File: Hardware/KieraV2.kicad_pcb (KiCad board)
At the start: 2 copper layers, 111 x 63.2 mm, 87 parts, among them J1 Conn_01x04_Male, J2 Conn_01x05_Male, SW1 SW_Rotary2x4, SW2 SW_Rotary2x4, SW3 SW_Push, SW4 SW_Push, SW5 SW_Push, SW6 SW_Push, SW7 SW_MEC_5G, U1 STM32L4P5RET6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

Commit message: aaaaa
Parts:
- removed MHe: MountingHole_3.2mm_M3, MountingHole:MountingHole_3.2mm_M3
- added MH6: MountingHole_3.2mm_M3, MountingHole:MountingHole_3.2mm_M3, F.Cu at (188.4, 96.0)
- renumbered MHe to MH2
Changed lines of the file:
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@@
     (tags "mounting hole 3.2mm no annular m3")
     (attr virtual)
-    (fp_text reference MHe (at -0.05 2.75) (layer F.SilkS)
+    (fp_text reference MH6 (at -0.05 2.75) (layer F.SilkS)
       (effects (font (size 1 1) (thickness 0.15)))
     )
@@
     (tags "mounting hole 4.5mm no annular")
     (attr virtual)
-    (fp_text reference MHe (at 0 6) (layer F.SilkS)
+    (fp_text reference MH2 (at 0 6) (layer F.SilkS)
       (effects (font (size 1 1) (thickness 0.15)))
     )

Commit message: added 6pin connector and somme labels
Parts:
- J2: value Conn_01x05_Male -> Conn_01x06_Male; footprint Connector_PinHeader_2.54mm:PinHeader_1x05_P2.54mm_Vertical -> Connector_PinHeader_2.54mm:PinHeader_1x06_P2.54mm_Vertical
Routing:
- net /SWO: track 0.00 -> 40.6 mm, vias 0 -> 2
- net /SW5: track 69.2 -> 71.6 mm
- net /SW6: track 71.0 -> 73.1 mm
- net GND: vias 45 -> 44
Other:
- board text added: "+5V"
- board text added: "CAN+"
- board text added: "CAN-"
- board text added: "SWO"

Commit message: added ground
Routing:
- net GND: vias 44 -> 49
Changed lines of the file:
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@@
     (thickness 1.6)
     (drawings 31)
-    (tracks 535)
+    (tracks 540)
     (zones 0)
     (modules 87)
@@
     (pcbplotparams
       (layerselection 0x010fc_ffffffff)
-      (usegerberextensions false)
+      (usegerberextensions true)
       (usegerberattributes true)
       (usegerberadvancedattributes true)
-      (creategerberjobfile true)
+      (creategerberjobfile false)
       (excludeedgelayer true)
       (linewidth 0.100000)
@@
       (psa4output false)
       (plotreference true)
-      (plotvalue true)
+      (plotvalue false)
       (plotinvisibletext false)
       (padsonsilk false)
-      (subtractmaskfromsilk false)
+      (subtractmaskfromsilk true)
       (outputformat 1)
       (mirror false)
-      (drillshape 1)
+      (drillshape 0)
       (scaleselection 1)
-      (outputdirectory ""))
+      (outputdirectory "SteeringWheelGerber/"))
   )
   (net 0 "")
@@
       (effects (font (size 1 1) (thickness 0.15)))
     )
-    (fp_text user %R (at 0 6.35) (layer F.Fab)
-      (effects (font (size 1 1) (thickness 0.15)))
-    )
     (fp_line (start -0.635 -1.27) (end 1.27 -1.27) (layer F.Fab) (width 0.1))
     (fp_line (start 1.27 -1.27) (end 1.27 13.97) (layer F.Fab) (width 0.1))
@@
     (fp_line (start 1.8 14.5) (end 1.8 -1.8) (layer F.CrtYd) (width 0.05))
     (fp_line (start 1.8 -1.8) (end -1.8 -1.8) (layer F.CrtYd) (width 0.05))
+    (fp_text user %R (at 0 6.35) (layer F.Fab)
+      (effects (font (size 1 1) (thickness 0.15)))
+    )
     (pad 6 thru_hole oval (at 0 12.7 270) (size 1.7 1.7) (drill 1) (layers *.Cu *.Mask)
       (net 45 /SWO))
@@
     (pad 2 thru_hole circle (at 4.2 0 270) (size 1.85 1.85) (drill 0.85) (layers *.Cu *.Mask)
       (net 89 /CAN+))
-    (pad 1 thru_hole roundrect (at 0 0 270) (size 1.85 1.85) (drill 0.85) (layers *.Cu *.Mask) (roundrect_rratio 0.135135)
+    (pad 1 thru_hole roundrect (at 0 0 270) (size 1.85 1.85) (drill 0.85) (layers *.Cu *.Mask) (roundrect_rratio 0.1351345945945946)
       (net 9 +5V))
     (model ${KISYS3DMOD}/Connector_Wire.3dshapes/SolderWire-0.25sqmm_1x04_P4.2mm_D0.65mm_OD1.7mm_Relief.wrl
@@
       (effects (font (size 0.5 0.5) (thickness 0.08)))
     )
-    (pad 2 smd roundrect (at 0.9625 0) (size 1.325 1.3) (layers F.Cu F.Paste F.Mask) (roundrect_rratio 0.192308)
+    (pad 2 smd roundrect (at 0.9625 0) (size 1.325 1.3) (layers F.Cu F.Paste F.Mask) (roundrect_rratio 0.1923076923076923)
       (net 95 "Net-(D7-Pad2)"))
-    (pad 1 smd roundrect (at -0.9625 0) (size 1.325 1.3) (layers F.Cu F.Paste F.Mask) (roundrect_rratio 0.192308)
+    (pad 1 smd roundrect (at -0.9625 0) (size 1.325 1.3) (layers F.Cu F.Paste F.Mask) (roundrect_rratio 0.1923076923076923)
       (net 8 +3V3))
     (model ${KISYS3DMOD}/Diode_SMD.3dshapes/D_0805_2012Metric_Castellated.wrl
@@
       (effects (font (size 0.5 0.5) (thickness 0.08)))
     )
-    (pad 2 smd roundrect (at 0.9625 0) (size 1.325 1.3) (layers F.Cu F.Paste F.Mask) (roundrect_rratio 0.192308)
+    (pad 2 smd roundrect (at 0.9625 0) (size 1.325 1.3) (layers F.Cu F.Paste F.Mask) (roundrect_rratio 0.1923076923076923)
       (net 94 "Net-(D6-Pad2)"))
-    (pad 1 smd roundrect (at -0.9625 0) (size 1.325 1.3) (layers F.Cu F.Paste F.Mask) (roundrect_rratio 0.192308)
+    (pad 1 smd roundrect (at -0.9625 0) (size 1.325 1.3) (layers F.Cu F.Paste F.Mask) (roundrect_rratio 0.1923076923076923)
       (net 8 +3V3))
     (model ${KISYS3DMOD}/Diode_SMD.3dshapes/D_0805_2012Metric_Castellated.wrl
@@
       (effects (font (size 0.5 0.5) (thickness 0.08)))
     )
-    (pad 2 smd roundrect (at 0.9625 0) (size 1.325 1.3) (layers F.Cu F.Paste F.Mask) (roundrect_rratio 0.192308)
+    (pad 2 smd roundrect (at 0.9625 0) (size 1.325 1.3) (layers F.Cu F.Paste F.Mask) (roundrect_rratio 0.1923076923076923)
       (net 96 "Net-(D8-Pad2)"))
-    (pad 1 smd roundrect (at -0.9625 0) (size 1.325 1.3) (layers F.Cu F.Paste F.Mask) (roundrect_rratio 0.192308)
+    (pad 1 smd roundrect (at -0.9625 0) (size 1.325 1.3) (layers F.Cu F.Paste F.Mask) (roundrect_rratio 0.1923076923076923)
       (net 8 +3V3))
     (model ${KISYS3DMOD}/Diode_SMD.3dshapes/D_0805_2012Metric_Castellated.wrl
@@
       (effects (font (size 0.5 0.5) (thickness 0.08)))
     )
-    (pad 2 smd roundrect (at 0.9625 0) (size 1.325 1.3) (layers F.Cu F.Paste F.Mask) (roundrect_rratio 0.192308)
+    (pad 2 smd roundrect (at 0.9625 0) (size 1.325 1.3) (layers F.Cu F.Paste F.Mask) (roundrect_rratio 0.1923076923076923)
       (net 93 "Net-(D5-Pad2)"))
-    (pad 1 smd roundrect (at -0.9625 0) (size 1.325 1.3) (layers F.Cu F.Paste F.Mask) (roundrect_rratio 0.192308)
+    (pad 1 smd roundrect (at -0.9625 0) (size 1.325 1.3) (layers F.Cu F.Paste F.Mask) (roundrect_rratio 0.1923076923076923)
       (net 8 +3V3))
     (model ${KISYS3DMOD}/Diode_SMD.3dshapes/D_0805_2012Metric_Castellated.wrl
@@
       (effects (font (size 0.5 0.5) (thickness 0.08)))
     )
-    (pad 2 smd roundrect (at 0.9625 0 90) (size 1.325 1.3) (layers F.Cu F.Paste F.Mask) (roundrect_rratio 0.192308)
+    (pad 2 smd roundrect (at 0.9625 0 90) (size 1.325 1.3) (layers F.Cu F.Paste F.Mask) (roundrect_rratio 0.1923076923076923)
       (net 8 +3V3))
-    (pad 1 smd roundrect (at -0.9625 0 90) (size 1.325 1.3) (layers F.Cu F.Paste F.Mask) (roundrect_rratio 0.192308)
+    (pad 1 smd roundrect (at -0.9625 0 90) (size 1.325 1.3) (layers F.Cu F.Paste F.Mask) (roundrect_rratio 0.1923076923076923)
       (net 13 "Net-(D1-Pad1)"))
     (model ${KISYS3DMOD}/Diode_SMD.3dshapes/D_0805_2012Metric_Castellated.wrl
@@
   (via (at 106.1 148.625) (size 0.8) (drill 0.4) (layers F.Cu B.Cu) (net 1))
   (via (at 106.775 125.9) (size 0.8) (drill 0.4) (layers F.Cu B.Cu) (net 1))
+  (via (at 154.225 131.05) (size 0.8) (drill 0.4) (layers F.Cu B.Cu) (net 1))
+  (via (at 151.9 129.125) (size 0.8) (drill 0.4) (layers F.Cu B.Cu) (net 1))
+  (via (at 154.325 121.325) (size 0.8) (drill 0.4) (layers F.Cu B.Cu) (net 1))
+  (via (at 155.5 122.15) (size 0.8) (drill 0.4) (layers F.Cu B.Cu) (net 1))
+  (via (at 163.35 131.925) (size 0.8) (drill 0.4) (layers F.Cu B.Cu) (net 1))
   (segment (start 152.525 104.775) (end 152.85 105.1) (width 0.25) (layer F.Cu) (net 2))
   (segment (start 151.05 104.775) (end 152.525 104.775) (width 0.25) (layer F.Cu) (net 2))

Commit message: more
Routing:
- net GND: vias 49 -> 99

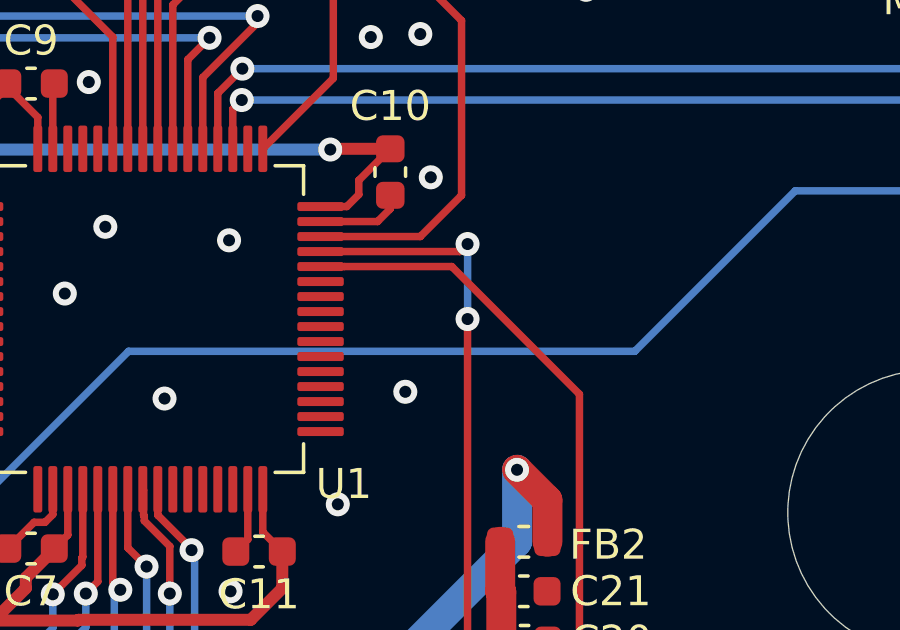
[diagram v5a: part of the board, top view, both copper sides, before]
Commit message: can on pcb updated
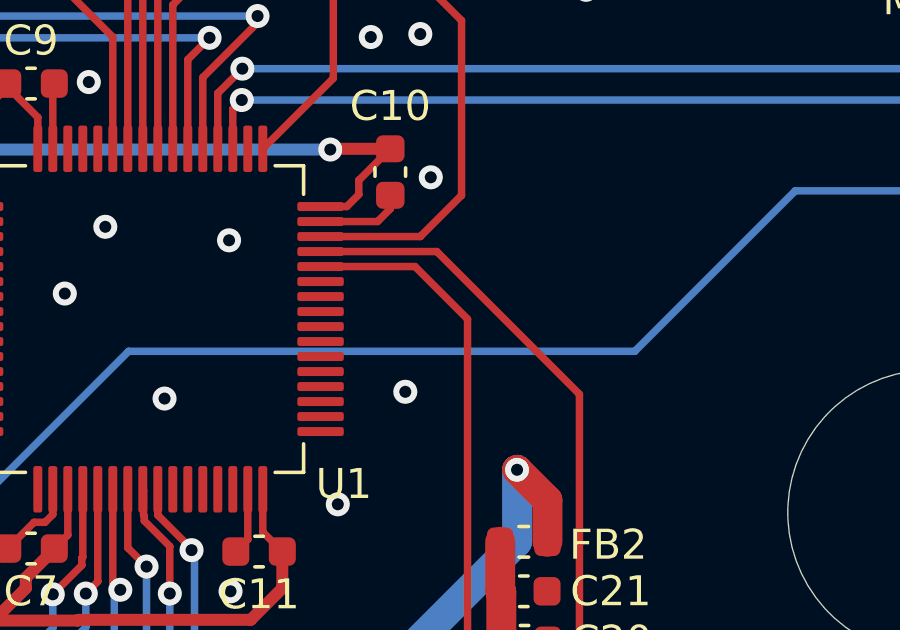
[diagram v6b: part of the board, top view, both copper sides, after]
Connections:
- U1 pad 44: /CAN_TX -> /CAN_RX
- U1 pad 45: /CAN_RX -> /CAN_TX
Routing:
- net /CAN_RX: track 20.5 -> 18.5 mm, vias 2 -> 0

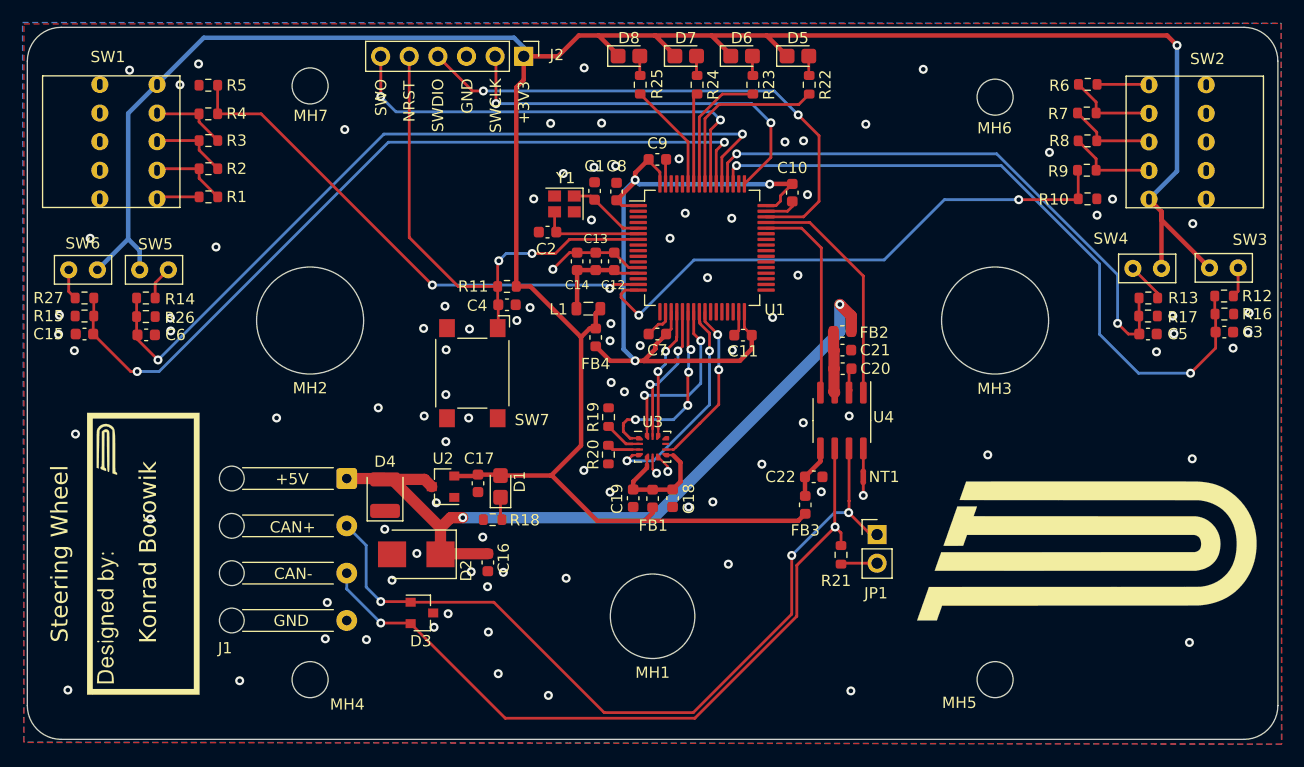
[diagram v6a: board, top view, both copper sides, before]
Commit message: redesigned pcb
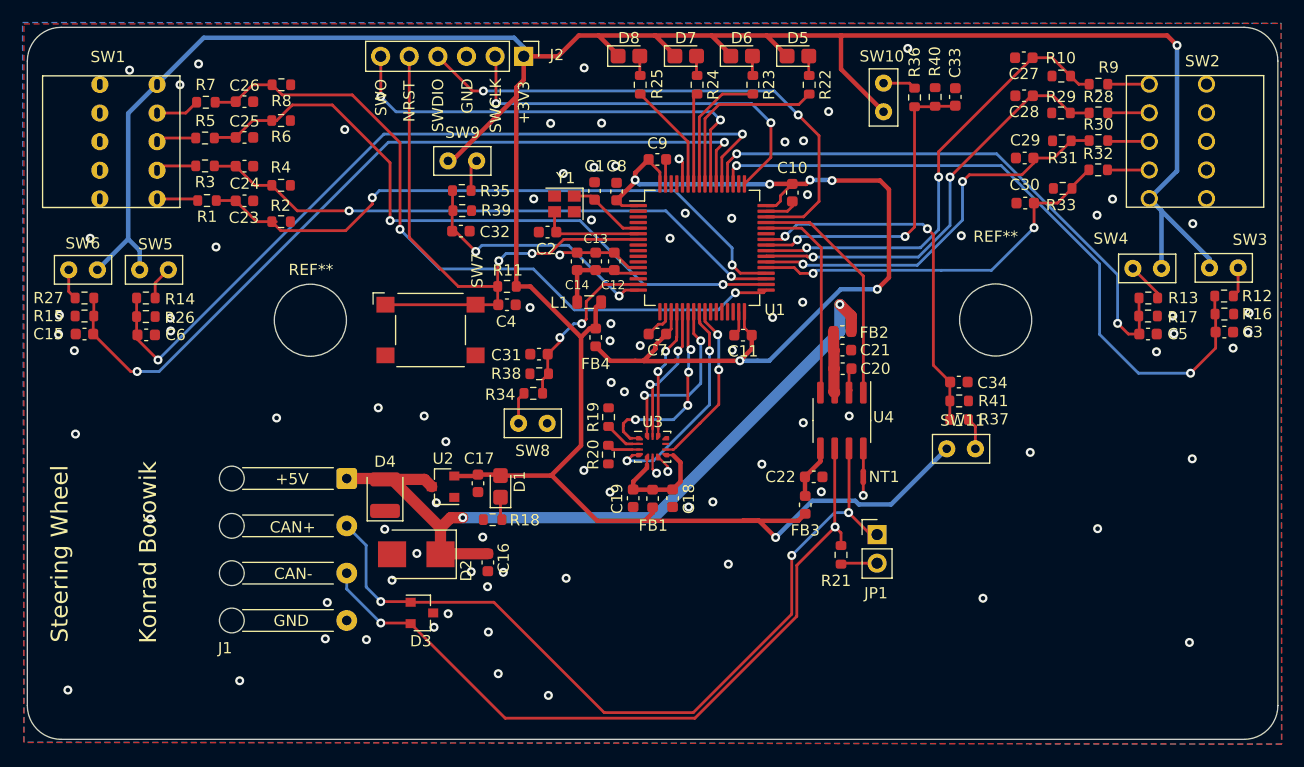
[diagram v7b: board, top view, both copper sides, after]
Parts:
- removed G***: LOGO, Logos:SignatureBox25mm
- removed G***: LOGO, Logos:PUTM_LOGO_35mm
- removed MH1: MountingHole_7.5mm, MountingHole:MountingHole_7.5mm
- removed MH2, MH3: MountingHole_9.5mm, MountingHole:MountingHole_9.5mm
- removed MH4, MH5, MH6, MH7: MountingHole_3.2mm_M3, MountingHole:MountingHole_3.2mm_M3
- added C23: 100nF, Capacitor_SMD:C_0603_1608Metric, F.Cu at (121.8, 105.2)
- added C24: 100nF, Capacitor_SMD:C_0603_1608Metric, F.Cu at (121.8, 102.1)
- added C25: 100nF, Capacitor_SMD:C_0603_1608Metric, F.Cu at (121.8, 99.6)
- added C26: 100nF, Capacitor_SMD:C_0603_1608Metric, F.Cu at (121.8, 96.4)
- added C27: 100nF, Capacitor_SMD:C_0603_1608Metric, F.Cu at (190.9, 92.5)
- added C28: 100nF, Capacitor_SMD:C_0603_1608Metric, F.Cu at (191.0, 95.9)
- added C29: 100nF, Capacitor_SMD:C_0603_1608Metric, F.Cu at (191.0, 101.4)
- added C30: 100nF, Capacitor_SMD:C_0603_1608Metric, F.Cu at (191.1, 105.4)
- added C31: 100nF, Capacitor_SMD:C_0603_1608Metric, F.Cu at (147.9, 118.8)
- added C32: 100nF, Capacitor_SMD:C_0603_1608Metric, F.Cu at (141.0, 107.9)
- added C33: 100nF, Capacitor_SMD:C_0603_1608Metric, F.Cu at (184.9, 96.0)
- added C34: 100nF, Capacitor_SMD:C_0603_1608Metric, F.Cu at (185.2, 121.3)
- added R28: 1k, Resistor_SMD:R_0603_1608Metric, F.Cu at (197.6, 97.4)
- added R29: 10k, Resistor_SMD:R_0603_1608Metric, F.Cu at (194.2, 97.4)
- added R30: 1k, Resistor_SMD:R_0603_1608Metric, F.Cu at (197.6, 99.8)
- added R31: 10k, Resistor_SMD:R_0603_1608Metric, F.Cu at (194.3, 99.9)
- added R32: 1k, Resistor_SMD:R_0603_1608Metric, F.Cu at (197.6, 102.5)
- added R33: 10k, Resistor_SMD:R_0603_1608Metric, F.Cu at (194.4, 104.1)
- added R34: 1k, Resistor_SMD:R_0603_1608Metric, F.Cu at (147.4, 122.3)
- added R35: 1k, Resistor_SMD:R_0603_1608Metric, F.Cu at (141.1, 104.3)
- added R36: 1k, Resistor_SMD:R_0603_1608Metric, F.Cu at (181.2, 96.0)
- added R37: 1k, Resistor_SMD:R_0603_1608Metric, F.Cu at (185.2, 124.6)
- added R38: 10k, Resistor_SMD:R_0603_1608Metric, F.Cu at (147.9, 120.5)
- added R39: 10k, Resistor_SMD:R_0603_1608Metric, F.Cu at (141.1, 106.1)
- added R40: 10k, Resistor_SMD:R_0603_1608Metric, F.Cu at (183.1, 96.0)
- added R41: 10k, Resistor_SMD:R_0603_1608Metric, F.Cu at (185.2, 123.0)
- added REF**: MountingHole_6.4mm_M6, MountingHole:MountingHole_6.4mm_M6, F.Cu at (127.6, 115.8)
- added REF**: MountingHole_6.4mm_M6, MountingHole:MountingHole_6.4mm_M6, F.Cu at (188.4, 115.8)
- added SW10: SW_Push, Button_Switch_THT:MyPushbuttonSwitch, F.Cu at (178.5, 96.0)
- added SW11: SW_Push, Button_Switch_THT:MyPushbuttonSwitch, F.Cu at (185.4, 127.2)
- added SW8: SW_Push, Button_Switch_THT:MyPushbuttonSwitch, F.Cu at (147.4, 125.0)
- added SW9: SW_Push, Button_Switch_THT:MyPushbuttonSwitch, F.Cu at (141.1, 101.7)
- R1: value 22k -> 1k
- R2: value 1k97 -> 10k
- R3: value 680 -> 1k
- R4: value 150 -> 10k
- R5: value 10k -> 1k
- R6: value 22k -> 10k
- R7: value 1k97 -> 1k
- R8: value 680 -> 10k
- R9: value 150 -> 1k
- moved R7 78.2 mm to (118.3, 96.5)
- moved R8 71.7 mm to (125.0, 94.9)
- moved R6 71.7 mm to (125.0, 98.1)
- moved R10 11.1 mm to (194.3, 94.1), turned to 0 degrees
- moved R4 9.05 mm to (125.0, 103.8), turned to 180 degrees
- moved R2 7.98 mm to (125.0, 107.0), turned to 180 degrees
- moved R9 7.70 mm to (197.6, 94.8), turned to 0 degrees
- moved SW7 5.33 mm to (138.3, 116.7), turned to 0 degrees
- moved R5 4.69 mm to (118.3, 99.6), turned to 180 degrees
- moved R3 2.27 mm to (118.3, 102.1), turned to 180 degrees
- moved L1 0.59 mm to (152.4, 114.2)
- moved R1 0.35 mm to (118.5, 105.2), turned to 180 degrees
- moved SW2 0.06 mm to (204.6, 99.9)
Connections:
- R1 pad 1: Net-(R1-Pad1) -> /SW1_4
- R10 pad 2: /SW2 -> /SW2_4
- R2 pad 1: Net-(R1-Pad2) -> GND
- R2 pad 2: Net-(R2-Pad2) -> /SW1_4
- R3 pad 1: Net-(R2-Pad2) -> /SW1_3
- R4 pad 1: Net-(R3-Pad2) -> GND
- R4 pad 2: /SW1 -> /SW1_3
- R5 pad 1: GND -> /SW1_2
- R5 pad 2: /SW1 -> Net-(R5-Pad2)
- R6 pad 1: Net-(R6-Pad1) -> GND
- R6 pad 2: Net-(R6-Pad2) -> /SW1_2
- R7 pad 1: Net-(R6-Pad2) -> /SW1_1
- R8 pad 1: Net-(R7-Pad2) -> GND
- R8 pad 2: Net-(R8-Pad2) -> /SW1_1
- R9 pad 1: Net-(R8-Pad2) -> /SW2_4
- R9 pad 2: /SW2 -> Net-(R9-Pad2)
- SW1 pad 2: Net-(R3-Pad2) -> Net-(R7-Pad2)
- SW1 pad 3: Net-(R2-Pad2) -> Net-(R5-Pad2)
- SW1 pad 4: Net-(R1-Pad2) -> Net-(R3-Pad2)
- SW1 pad 5: Net-(R1-Pad1) -> Net-(R1-Pad2)
- SW2 pad 2: Net-(R8-Pad2) -> Net-(R32-Pad2)
- SW2 pad 3: Net-(R7-Pad2) -> Net-(R30-Pad2)
- SW2 pad 4: Net-(R6-Pad2) -> Net-(R28-Pad2)
- SW2 pad 5: Net-(R6-Pad1) -> Net-(R9-Pad2)
- U1 pad 15: /SW1 -> /SW7
- U1 pad 16: /SW2 -> /SW8
- U1 pad 33: Net-(U1-Pad33) -> /SW1_1
- U1 pad 34: Net-(U1-Pad34) -> /SW1_2
- U1 pad 35: Net-(U1-Pad35) -> /SW1_3
- U1 pad 36: Net-(U1-Pad36) -> /SW1_4
- U1 pad 37: Net-(U1-Pad37) -> /SW2_1
- U1 pad 38: Net-(U1-Pad38) -> /SW2_2
- U1 pad 39: Net-(U1-Pad39) -> /SW2_3
- U1 pad 40: Net-(U1-Pad40) -> /SW2_4
- U1 pad 41: Net-(U1-Pad41) -> /SW9
- U1 pad 42: Net-(U1-Pad42) -> /SW10
- U1 pad 60: Net-(U1-Pad60) -> GND
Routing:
- net /SW1_1: track 0.00 -> 63.0 mm, vias 0 -> 2
- net /SW1_2: track 0.00 -> 59.8 mm, vias 0 -> 2
- net /SW1_4: track 0.00 -> 56.0 mm, vias 0 -> 2
- net /SW1_3: track 0.00 -> 53.1 mm, vias 0 -> 2
- net /SW2: track 50.0 -> 0.00 mm, vias 2 -> 0
- net /SW1: track 46.4 -> 0.00 mm, vias 2 -> 0
- net /SW2_4: track 0.00 -> 41.0 mm, vias 0 -> 2
- net +3V3: track 234.7 -> 275.0 mm, vias 1 -> 2
- net /SW2_3: track 0.00 -> 37.9 mm, vias 0 -> 2
- net /SW2_2: track 0.00 -> 35.7 mm, vias 0 -> 2
- net /SW2_1: track 0.00 -> 34.1 mm, vias 0 -> 2
- net /SW10: track 0.00 -> 33.0 mm, vias 0 -> 2
- net /SW9: track 0.00 -> 28.2 mm, vias 0 -> 2
- net /SW8: track 0.00 -> 23.2 mm, vias 0 -> 2
- net /+3V3_uC: track 67.7 -> 84.0 mm, vias 3 -> 6
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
